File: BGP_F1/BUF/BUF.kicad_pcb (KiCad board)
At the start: 2 copper layers, 28 x 24 mm, 21 parts, among them P1 CONN_01X02, P2 CONN_01X05, P3 CONN_01X12, U1 MC33178

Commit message: New F0 Version
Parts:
- P2: footprint Connectors_Molex:Molex_MicroLatch-53253-0570_05x2.00mm_Straight -> Connectors_JST:JST_PH_B5B-PH-K_05x2.00mm_Straight
- moved P2 0.70 mm to (156.0, 97.7)
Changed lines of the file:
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@@
-    )
-  )
-  (module Connectors_Molex:Molex_MicroLatch-53253-0570_05x2.00mm_Straight (layer F.Cu)
-    (at 156 97 180)
-    (descr "Molex Micro-Latch connector, PN:53253-0570, top entry type, through hole")
-    (tags "conn molex micro latch")
-    (fp_text reference P2 (at -1.5 -2.3 180) (layer F.SilkS)
-      (effects (font (size 0.6 0.6) (thickness 0.15)))
-    )
-    (fp_text value CONN_01X05 (at 4 -3.5 180) (layer F.Fab) hide
-      (effects (font (size 0.6 0.6) (thickness 0.15)))
-    )
-    (fp_line (start -2.6 -2.1) (end -2.6 2.75) (layer F.CrtYd) (width 0.05))
-    (fp_line (start -2.6 2.75) (end 10.55 2.75) (layer F.CrtYd) (width 0.05))
-    (fp_line (start 10.55 2.75) (end 10.55 -2.1) (layer F.CrtYd) (width 0.05))
-    (fp_line (start 10.55 -2.1) (end -2.6 -2.1) (layer F.CrtYd) (width 0.05))
-    (fp_line (start -2.1 -1.6) (end -2.1 2.25) (layer F.SilkS) (width 0.15))
-    (fp_line (start -2.1 2.25) (end 10.1 2.25) (layer F.SilkS) (width 0.15))
-    (fp_line (start 10.1 2.25) (end 10.1 -1.6) (layer F.SilkS) (width 0.15))
-    (fp_line (start 10.1 -1.6) (end -2.1 -1.6) (layer F.SilkS) (width 0.15))
-    (fp_line (start 0 -2) (end -0.3 -2.6) (layer F.SilkS) (width 0.15))
-    (fp_line (start -0.3 -2.6) (end 0.3 -2.6) (layer F.SilkS) (width 0.15))
-    (fp_line (start 0.3 -2.6) (end 0 -2) (layer F.SilkS) (width 0.15))
-    (fp_line (start -2.1 0.8) (end -1.7 0.8) (layer F.SilkS) (width 0.15))
-    (fp_line (start 10.1 0.8) (end 9.7 0.8) (layer F.SilkS) (width 0.15))
-    (fp_line (start 4 -1.2) (end -1.7 -1.2) (layer F.SilkS) (width 0.15))
-    (fp_line (start -1.7 -1.2) (end -1.7 0) (layer F.SilkS) (width 0.15))
-    (fp_line (start -1.7 0) (end -1.3 0) (layer F.SilkS) (width 0.15))
-    (fp_line (start -1.3 0) (end -1.3 0.4) (layer F.SilkS) (width 0.15))
-    (fp_line (start -1.3 0.4) (end -1.7 0.4) (layer F.SilkS) (width 0.15))
-    (fp_line (start -1.7 0.4) (end -1.7 2.25) (layer F.SilkS) (width 0.15))
-    (fp_line (start 4 -1.2) (end 9.7 -1.2) (layer F.SilkS) (width 0.15))
-    (fp_line (start 9.7 -1.2) (end 9.7 0) (layer F.SilkS) (width 0.15))
-    (fp_line (start 9.7 0) (end 9.3 0) (layer F.SilkS) (width 0.15))
-    (fp_line (start 9.3 0) (end 9.3 0.4) (layer F.SilkS) (width 0.15))
-    (fp_line (start 9.3 0.4) (end 9.7 0.4) (layer F.SilkS) (width 0.15))
-    (fp_line (start 9.7 0.4) (end 9.7 2.25) (layer F.SilkS) (width 0.15))
-    (pad 1 thru_hole rect (at 0 0 180) (size 1.5 1.5) (drill 0.8) (layers *.Cu *.Mask)
-      (net 9 Earth))
-    (pad 2 thru_hole circle (at 2 0 180) (size 1.5 1.5) (drill 0.8) (layers *.Cu *.Mask)
-      (net 8 /OUT))
-    (pad 3 thru_hole circle (at 4 0 180) (size 1.5 1.5) (drill 0.8) (layers *.Cu *.Mask)
-      (net 10 /BUF_O))
-    (pad 4 thru_hole circle (at 6 0 180) (size 1.5 1.5) (drill 0.8) (layers *.Cu *.Mask)
-      (net 6 /Vref))
-    (pad 5 thru_hole circle (at 8 0 180) (size 1.5 1.5) (drill 0.8) (layers *.Cu *.Mask)
-      (net 11 /V+))
-    (model Connectors_Molex.3dshapes/Molex_MicroLatch-53253-0570_05x2.00mm_Straight.wrl
-      (at (xyz 0 0 0))
-      (scale (xyz 1 1 1))
-      (rotate (xyz 0 0 0))
     )
   )
@@
       (at (xyz 0 0 0))
       (scale (xyz 1 1 1))
+      (rotate (xyz 0 0 0))
+    )
+  )
+  (module Connectors_JST:JST_PH_B5B-PH-K_05x2.00mm_Straight (layer F.Cu)
+    (at 156 97.7 180)
+    (descr "JST PH series connector, B5B-PH-K, top entry type, through hole, Datasheet: http://www.jst-mfg.com/product/pdf/eng/ePH.pdf")
+    (tags "connector jst ph")
+    (fp_text reference P2 (at 10.8 2.6 180) (layer F.SilkS)
+      (effects (font (size 0.6 0.6) (thickness 0.15)))
+    )
+    (fp_text value CONN_01X05 (at 4 3.8 180) (layer F.Fab) hide
+      (effects (font (size 0.6 0.6) (thickness 0.15)))
+    )
+    (fp_line (start -2.05 -1.8) (end -2.05 2.9) (layer F.SilkS) (width 0.12))
+    (fp_line (start -2.05 2.9) (end 10.05 2.9) (layer F.SilkS) (width 0.12))
+    (fp_line (start 10.05 2.9) (end 10.05 -1.8) (layer F.SilkS) (width 0.12))
+    (fp_line (start 10.05 -1.8) (end -2.05 -1.8) (layer F.SilkS) (width 0.12))
+    (fp_line (start 0.5 -1.8) (end 0.5 -1.2) (layer F.SilkS) (width 0.12))
+    (fp_line (start 0.5 -1.2) (end -1.45 -1.2) (layer F.SilkS) (width 0.12))
+    (fp_line (start -1.45 -1.2) (end -1.45 2.3) (layer F.SilkS) (width 0.12))
+    (fp_line (start -1.45 2.3) (end 9.45 2.3) (layer F.SilkS) (width 0.12))
+    (fp_line (start 9.45 2.3) (end 9.45 -1.2) (layer F.SilkS) (width 0.12))
+    (fp_line (start 9.45 -1.2) (end 7.5 -1.2) (layer F.SilkS) (width 0.12))
+    (fp_line (start 7.5 -1.2) (end 7.5 -1.8) (layer F.SilkS) (width 0.12))
+    (fp_line (start -2.05 -0.5) (end -1.45 -0.5) (layer F.SilkS) (width 0.12))
+    (fp_line (start -2.05 0.8) (end -1.45 0.8) (layer F.SilkS) (width 0.12))
+    (fp_line (start 10.05 -0.5) (end 9.45 -0.5) (layer F.SilkS) (width 0.12))
+    (fp_line (start 10.05 0.8) (end 9.45 0.8) (layer F.SilkS) (width 0.12))
+    (fp_line (start -0.3 -1.8) (end -0.3 -2) (layer F.SilkS) (width 0.12))
+    (fp_line (start -0.3 -2) (end -0.6 -2) (layer F.SilkS) (width 0.12))
+    (fp_line (start -0.6 -2) (end -0.6 -1.8) (layer F.SilkS) (width 0.12))
+    (fp_line (start -0.3 -1.9) (end -0.6 -1.9) (layer F.SilkS) (width 0.12))
+    (fp_line (start 0.9 2.3) (end 0.9 1.8) (layer F.SilkS) (width 0.12))
+    (fp_line (start 0.9 1.8) (end 1.1 1.8) (layer F.SilkS) (width 0.12))
+    (fp_line (start 1.1 1.8) (end 1.1 2.3) (layer F.SilkS) (width 0.12))
+    (fp_line (start 1 2.3) (end 1 1.8) (layer F.SilkS) (width 0.12))
+    (fp_line (start 2.9 2.3) (end 2.9 1.8) (layer F.SilkS) (width 0.12))
+    (fp_line (start 2.9 1.8) (end 3.1 1.8) (layer F.SilkS) (width 0.12))
+    (fp_line (start 3.1 1.8) (end 3.1 2.3) (layer F.SilkS) (width 0.12))
+    (fp_line (start 3 2.3) (end 3 1.8) (layer F.SilkS) (width 0.12))
+    (fp_line (start 4.9 2.3) (end 4.9 1.8) (layer F.SilkS) (width 0.12))
+    (fp_line (start 4.9 1.8) (end 5.1 1.8) (layer F.SilkS) (width 0.12))
+    (fp_line (start 5.1 1.8) (end 5.1 2.3) (layer F.SilkS) (width 0.12))
+    (fp_line (start 5 2.3) (end 5 1.8) (layer F.SilkS) (width 0.12))
+    (fp_line (start 6.9 2.3) (end 6.9 1.8) (layer F.SilkS) (width 0.12))
+    (fp_line (start 6.9 1.8) (end 7.1 1.8) (layer F.SilkS) (width 0.12))
+    (fp_line (start 7.1 1.8) (end 7.1 2.3) (layer F.SilkS) (width 0.12))
+    (fp_line (start 7 2.3) (end 7 1.8) (layer F.SilkS) (width 0.12))
+    (fp_line (start -1.1 -2.1) (end -2.35 -2.1) (layer F.SilkS) (width 0.12))
+    (fp_line (start -2.35 -2.1) (end -2.35 -0.85) (layer F.SilkS) (width 0.12))
+    (fp_line (start -1.1 -2.1) (end -2.35 -2.1) (layer F.Fab) (width 0.1))
+    (fp_line (start -2.35 -2.1) (end -2.35 -0.85) (layer F.Fab) (width 0.1))
+    (fp_line (start -1.95 -1.7) (end -1.95 2.8) (layer F.Fab) (width 0.1))
+    (fp_line (start -1.95 2.8) (end 9.95 2.8) (layer F.Fab) (width 0.1))
+    (fp_line (start 9.95 2.8) (end 9.95 -1.7) (layer F.Fab) (width 0.1))
+    (fp_line (start 9.95 -1.7) (end -1.95 -1.7) (layer F.Fab) (width 0.1))
+    (fp_line (start -2.45 -2.2) (end -2.45 3.3) (layer F.CrtYd) (width 0.05))
+    (fp_line (start -2.45 3.3) (end 10.45 3.3) (layer F.CrtYd) (width 0.05))
+    (fp_line (start 10.45 3.3) (end 10.45 -2.2) (layer F.CrtYd) (width 0.05))
+    (fp_line (start 10.45 -2.2) (end -2.45 -2.2) (layer F.CrtYd) (width 0.05))
+    (fp_text user %R (at 4 1.5 180) (layer F.Fab) hide
+      (effects (font (size 0.6 0.6) (thickness 0.15)))
+    )
+    (pad 1 thru_hole rect (at 0 0 180) (size 1.2 1.7) (drill 0.75) (layers *.Cu *.Mask)
+      (net 9 Earth))
+    (pad 2 thru_hole oval (at 2 0 180) (size 1.2 1.7) (drill 0.75) (layers *.Cu *.Mask)
+      (net 8 /OUT))
+    (pad 3 thru_hole oval (at 4 0 180) (size 1.2 1.7) (drill 0.75) (layers *.Cu *.Mask)
+      (net 10 /BUF_O))
+    (pad 4 thru_hole oval (at 6 0 180) (size 1.2 1.7) (drill 0.75) (layers *.Cu *.Mask)
+      (net 6 /Vref))
+    (pad 5 thru_hole oval (at 8 0 180) (size 1.2 1.7) (drill 0.75) (layers *.Cu *.Mask)
+      (net 11 /V+))
+    (model ${KISYS3DMOD}/Connectors_JST.3dshapes/JST_PH_B5B-PH-K_05x2.00mm_Straight.wrl
+      (at (xyz 0 0 0))
+      (scale (xyz 1 1 1))

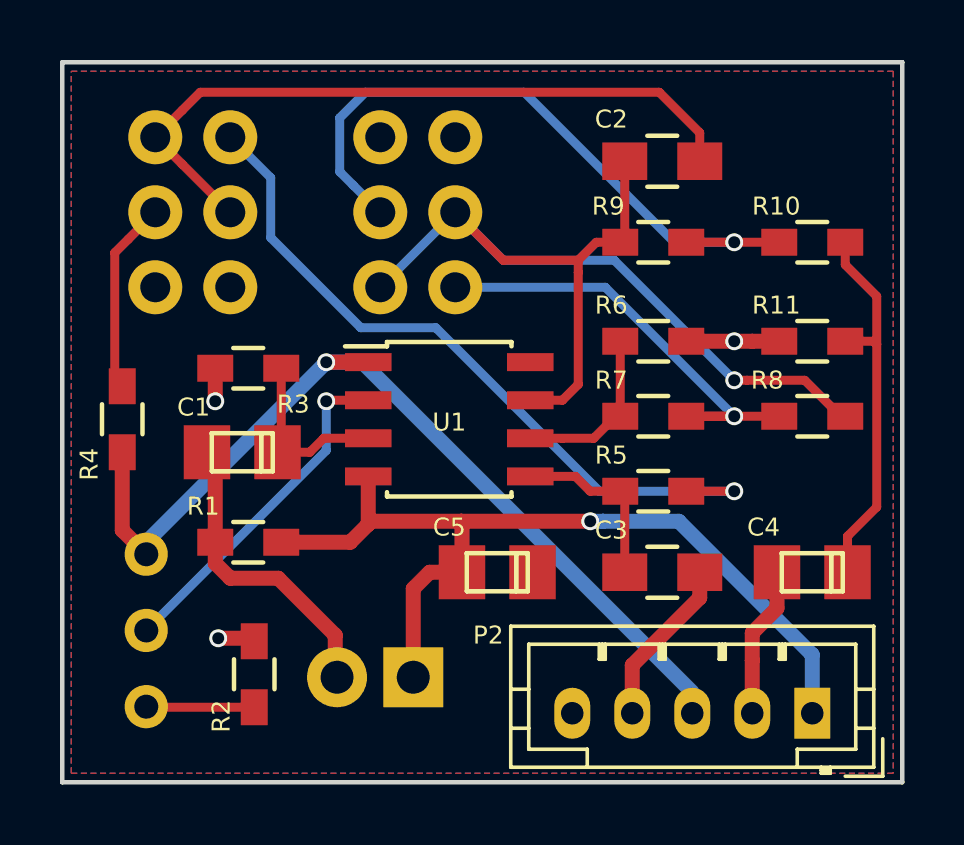
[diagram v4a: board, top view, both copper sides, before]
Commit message: F1 updates to reverse pots
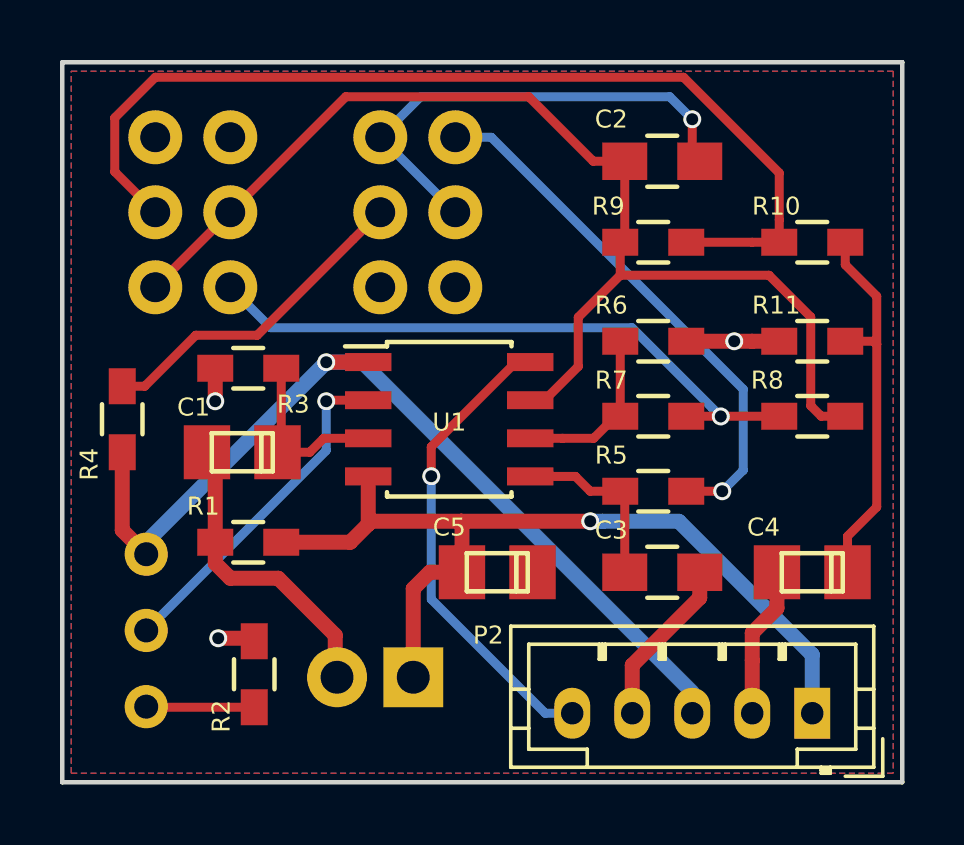
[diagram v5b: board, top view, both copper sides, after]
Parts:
- R1, R3: value 499k -> 470k
- R10, R11, R6, R7: value 15k -> 27k
- R2: value 2.49k -> 2.4k
- R4, R5: value 4.99k -> 4.7k
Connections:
- P3 pad 1: /PF1_1 -> /PG1_1
- P3 pad 10: /PG2_1 -> /PF2_1
- P3 pad 11: /PG1_1 -> /PF1_3
- P3 pad 12: /PG2_3 -> /PF3_3
- P3 pad 2: /PF1_2 -> /PG1_2
- P3 pad 3: /PF1_3 -> /PG1_3
- P3 pad 4: /PF2_1 -> /PG2_1
- P3 pad 5: /PF1_3 -> /PG1_1
- P3 pad 6: /PF3_3 -> /PG2_3
- P3 pad 7: /PG1_1 -> /PF1_1
- P3 pad 8: /PG1_2 -> /PF1_2
- P3 pad 9: /PG1_3 -> /PF1_3
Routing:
- net /V+: track 0.00 -> 15.8 mm, vias 0 -> 1
- net /PG1_2: track 22.5 -> 33.1 mm, vias 1 -> 0
- net /PF1_3: track 23.8 -> 16.4 mm, vias 0 -> 1
- net /PF3_3: track 24.5 -> 18.1 mm
- net /PG1_1: track 34.6 -> 40.3 mm, vias 1 -> 0
- net /PG2_1: track 15.8 -> 21.2 mm
- net /PF1_2: track 6.46 -> 11.4 mm
